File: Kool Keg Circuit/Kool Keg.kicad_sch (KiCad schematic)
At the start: 1 part, among them J1 Conn_01x02_Male

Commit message: Consolidating yet again
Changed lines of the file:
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@@
   (junction (at 176.53 55.88) (diameter 0) (color 0 0 0 0)
   )
+  (junction (at 67.31 55.88) (diameter 0) (color 0 0 0 0)
+  )
   (junction (at 59.69 55.88) (diameter 0) (color 0 0 0 0)
   )
@@
     (stroke (width 0) (type default) (color 0 0 0 0))
   )
+  (wire (pts (xy 67.31 55.88) (xy 129.54 55.88))
+    (stroke (width 0) (type default) (color 0 0 0 0))
+  )
   (wire (pts (xy 44.45 58.42) (xy 59.69 58.42))
     (stroke (width 0) (type default) (color 0 0 0 0))
@@
     (stroke (width 0) (type default) (color 0 0 0 0))
   )
+  (wire (pts (xy 59.69 55.88) (xy 67.31 55.88))
+    (stroke (width 0) (type default) (color 0 0 0 0))
+  )
   (wire (pts (xy 130.81 120.65) (xy 160.02 120.65))
     (stroke (width 0) (type default) (color 0 0 0 0))
@@
   )
   (wire (pts (xy 77.47 83.82) (xy 172.72 83.82))
-    (stroke (width 0) (type default) (color 0 0 0 0))
-  )
-  (wire (pts (xy 59.69 55.88) (xy 129.54 55.88))
     (stroke (width 0) (type default) (color 0 0 0 0))
   )
@@
     )
     (property "Datasheet" "" (id 3) (at 187.96 49.53 0)
+      (effects (font (size 1.27 1.27)) hide)
+    )
+    (pin "1")
+  )
+  (symbol (lib_id "power:PWR_FLAG") (at 67.31 55.88 0) (unit 1)
+    (in_bom yes) (on_board yes)
+    (property "Reference" "#FLG0101" (id 0) (at 67.31 53.975 0)
+      (effects (font (size 1.27 1.27)) hide)
+    )
+    (property "Value" "PWR_FLAG" (id 1) (at 63.5 52.07 0)
+      (effects (font (size 1.27 1.27)) (justify left))
+    )
+    (property "Footprint" "" (id 2) (at 67.31 55.88 0)
+      (effects (font (size 1.27 1.27)) hide)
+    )
+    (property "Datasheet" "~" (id 3) (at 67.31 55.88 0)
       (effects (font (size 1.27 1.27)) hide)
     )
@@
   )
   (symbol_instances
-    (path "/4be3bbc9-041b-406b-8a57-e104c00209e5/73ddb352-b11a-470f-a2de-747848aa5039"
+    (path "/3cd19ba5-e8f7-41de-8164-9647abe836bd"
       (reference "#FLG0101") (unit 1) (value "PWR_FLAG") (footprint "")
-    )
-    (path "/4be3bbc9-041b-406b-8a57-e104c00209e5/3553280e-8e79-46c6-b567-b74f146c5661"
-      (reference "#FLG0102") (unit 1) (value "PWR_FLAG") (footprint "")
     )
     (path "/61b5ec96-7a3b-40f2-a62b-7e3d165d26d5/0bd8cb44-e446-4f6a-b662-1042ca485aec"
       (reference "#FLG0103") (unit 1) (value "PWR_FLAG") (footprint "")
     )
+    (path "/4be3bbc9-041b-406b-8a57-e104c00209e5/1a1063da-ce01-4515-b674-bc8c663ad34f"
+      (reference "#FLG0104") (unit 1) (value "PWR_FLAG") (footprint "")
+    )
     (path "/c838e70f-cadd-4e22-8277-d73654eb9fff"

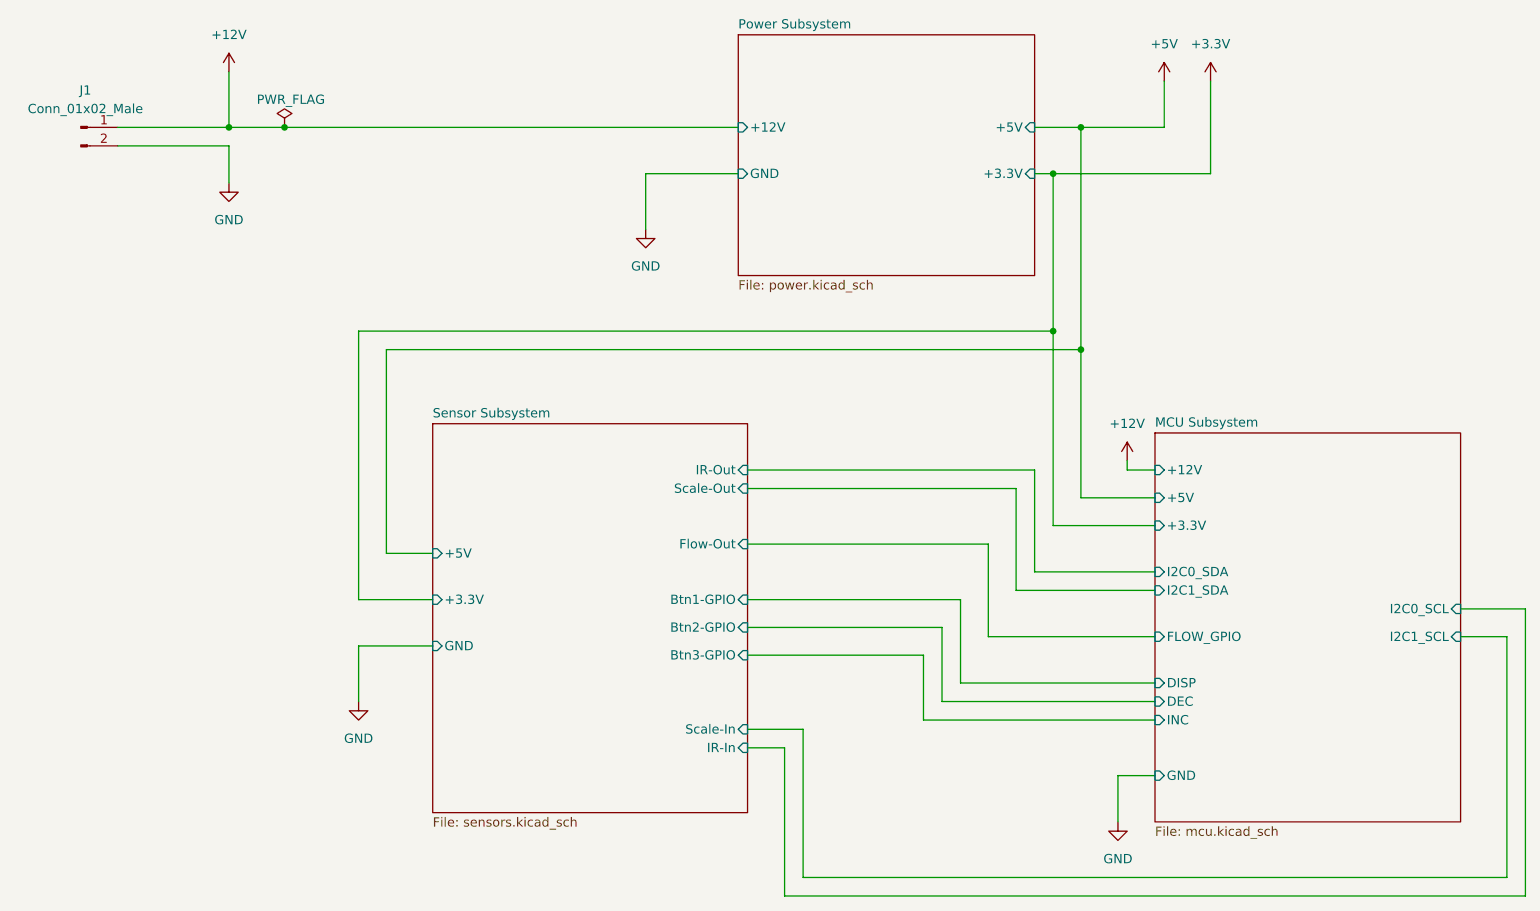
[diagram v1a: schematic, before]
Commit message: Update footprints, init layout
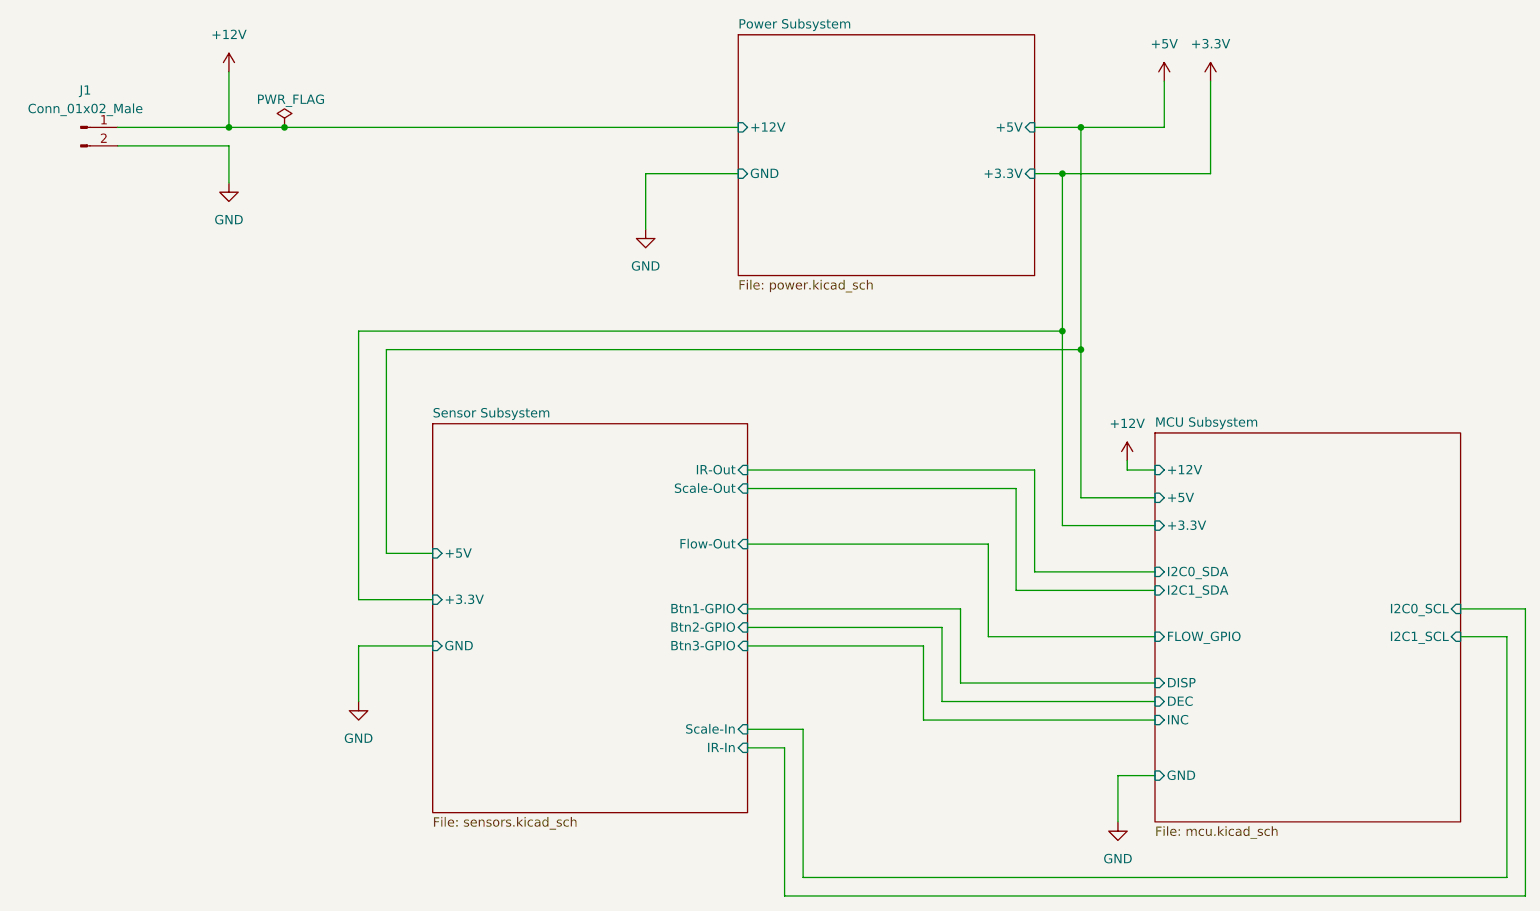
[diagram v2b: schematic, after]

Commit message: Update PCB
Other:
- sheet MCU Subsystem ports: added WEIGHT_CLK, WEIGHT_DATA; removed none
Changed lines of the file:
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@@
+    (stroke (width 0) (type default) (color 0 0 0 0))
+  )
+  (wire (pts (xy 138.43 138.43) (xy 138.43 158.75))
     (stroke (width 0) (type default) (color 0 0 0 0))
   )
@@
     (stroke (width 0) (type default) (color 0 0 0 0))
   )
-  (wire (pts (xy 138.43 158.75) (xy 138.43 138.43))
-    (stroke (width 0) (type default) (color 0 0 0 0))
-  )
   (wire (pts (xy 176.53 55.88) (xy 176.53 86.36))
     (stroke (width 0) (type default) (color 0 0 0 0))
@@
     (stroke (width 0) (type default) (color 0 0 0 0))
   )
-  (wire (pts (xy 167.64 119.38) (xy 186.69 119.38))
-    (stroke (width 0) (type default) (color 0 0 0 0))
-  )
   (wire (pts (xy 163.83 125.73) (xy 186.69 125.73))
     (stroke (width 0) (type default) (color 0 0 0 0))
@@
     (stroke (width 0) (type default) (color 0 0 0 0))
   )
-  (wire (pts (xy 130.81 105.41) (xy 167.64 105.41))
-    (stroke (width 0) (type default) (color 0 0 0 0))
-  )
   (wire (pts (xy 182.88 102.87) (xy 186.69 102.87))
     (stroke (width 0) (type default) (color 0 0 0 0))
@@
     (stroke (width 0) (type default) (color 0 0 0 0))
   )
+  (wire (pts (xy 166.37 121.92) (xy 186.69 121.92))
+    (stroke (width 0) (type default) (color 0 0 0 0))
+  )
   (wire (pts (xy 237.49 121.92) (xy 237.49 161.29))
     (stroke (width 0) (type default) (color 0 0 0 0))
@@
     (stroke (width 0) (type default) (color 0 0 0 0))
   )
+  (wire (pts (xy 166.37 105.41) (xy 166.37 121.92))
+    (stroke (width 0) (type default) (color 0 0 0 0))
+  )
   (wire (pts (xy 44.45 58.42) (xy 59.69 58.42))
     (stroke (width 0) (type default) (color 0 0 0 0))
@@
     (stroke (width 0) (type default) (color 0 0 0 0))
   )
-  (wire (pts (xy 234.95 125.73) (xy 234.95 158.75))
-    (stroke (width 0) (type default) (color 0 0 0 0))
-  )
   (wire (pts (xy 59.69 55.88) (xy 59.69 48.26))
     (stroke (width 0) (type default) (color 0 0 0 0))
@@
     (stroke (width 0) (type default) (color 0 0 0 0))
   )
+  (wire (pts (xy 138.43 158.75) (xy 233.68 158.75))
+    (stroke (width 0) (type default) (color 0 0 0 0))
+  )
   (wire (pts (xy 129.54 62.23) (xy 116.84 62.23))
     (stroke (width 0) (type default) (color 0 0 0 0))
   )
-  (wire (pts (xy 234.95 158.75) (xy 138.43 158.75))
-    (stroke (width 0) (type default) (color 0 0 0 0))
-  )
   (wire (pts (xy 154.94 137.16) (xy 186.69 137.16))
     (stroke (width 0) (type default) (color 0 0 0 0))
@@
     (stroke (width 0) (type default) (color 0 0 0 0))
   )
+  (wire (pts (xy 130.81 105.41) (xy 166.37 105.41))
+    (stroke (width 0) (type default) (color 0 0 0 0))
+  )
   (wire (pts (xy 81.28 86.36) (xy 176.53 86.36))
     (stroke (width 0) (type default) (color 0 0 0 0))
   )
-  (wire (pts (xy 138.43 138.43) (xy 130.81 138.43))
+  (wire (pts (xy 233.68 158.75) (xy 233.68 129.54))
     (stroke (width 0) (type default) (color 0 0 0 0))
   )
@@
     (stroke (width 0) (type default) (color 0 0 0 0))
   )
-  (wire (pts (xy 167.64 105.41) (xy 167.64 119.38))
-    (stroke (width 0) (type default) (color 0 0 0 0))
-  )
-  (wire (pts (xy 228.6 125.73) (xy 234.95 125.73))
+  (wire (pts (xy 130.81 138.43) (xy 138.43 138.43))
     (stroke (width 0) (type default) (color 0 0 0 0))
   )
@@
   )
   (wire (pts (xy 87.63 127) (xy 77.47 127))
+    (stroke (width 0) (type default) (color 0 0 0 0))
+  )
+  (wire (pts (xy 233.68 129.54) (xy 228.6 129.54))
     (stroke (width 0) (type default) (color 0 0 0 0))
   )
@@
       (effects (font (size 1.27 1.27)) (justify left))
     )
-  )
+    (pin "WEIGHT_DATA" input (at 186.69 121.92 180)
+      (effects (font (size 1.27 1.27)) (justify left))
+    )
+    (pin "WEIGHT_CLK" input (at 228.6 129.54 0)
+      (effects (font (size 1.27 1.27)) (justify right))
+    )
+  )
